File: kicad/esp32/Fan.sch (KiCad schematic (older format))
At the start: 3 parts, among them P18 Fan, Q6 IRFML8244

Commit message: 自動配線成功
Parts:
- renumbered P18 to P17
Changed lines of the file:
@@
 $Descr A4 11693 8268
 encoding utf-8
-Sheet 13 13
+Sheet 13 14
 Title ""
 Date ""
@@
 $EndComp
 $Comp
-L GND #PWR068
+L GND #PWR065
 U 1 1 58AB90DB
 P 5150 5300
-F 0 "#PWR068" H 5150 5050 50  0001 C CNN
+F 0 "#PWR065" H 5150 5050 50  0001 C CNN
 F 1 "GND" H 5150 5150 50  0000 C CNN
 F 2 "" H 5150 5300 50  0000 C CNN
@@
 Connection ~ 4750 4800
 $Comp
-L GND #PWR069
+L GND #PWR066
 U 1 1 58AB9100
 P 4750 5300
-F 0 "#PWR069" H 4750 5050 50  0001 C CNN
+F 0 "#PWR066" H 4750 5050 50  0001 C CNN
 F 1 "GND" H 4750 5150 50  0000 C CNN
 F 2 "" H 4750 5300 50  0000 C CNN
@@
 	4750 5300 4750 5200
 $Comp
-L CONN_01X02 P18
+L CONN_01X02 P17
 U 1 1 58AB920C
 P 5450 4350
-F 0 "P18" H 5450 4500 50  0000 C CNN
+F 0 "P17" H 5450 4500 50  0000 C CNN
 F 1 "Fan" V 5550 4350 50  0000 C CNN
 F 2 "mouse:SMD_conn_2" H 5450 4350 50  0001 C CNN
@@
 $EndComp
 $Comp
-L +BATT #PWR070
+L +BATT #PWR067
 U 1 1 58AB927D
 P 5150 4100
-F 0 "#PWR070" H 5150 3950 50  0001 C CNN
+F 0 "#PWR067" H 5150 3950 50  0001 C CNN
 F 1 "+BATT" H 5150 4240 50  0000 C CNN
 F 2 "" H 5150 4100 50  0000 C CNN

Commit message: 更新
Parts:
- renumbered R34 to R33
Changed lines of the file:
@@
 $EndComp
 $Comp
-L GND #PWR065
+L GND #PWR064
 U 1 1 58AB90DB
 P 5150 5300
-F 0 "#PWR065" H 5150 5050 50  0001 C CNN
+F 0 "#PWR064" H 5150 5050 50  0001 C CNN
 F 1 "GND" H 5150 5150 50  0000 C CNN
 F 2 "" H 5150 5300 50  0000 C CNN
@@
 	5150 5000 5150 5300
 $Comp
-L R R34
+L R R33
 U 1 1 58AB90F7
 P 4750 5050
-F 0 "R34" V 4830 5050 50  0000 C CNN
+F 0 "R33" V 4830 5050 50  0000 C CNN
 F 1 "10k" V 4750 5050 50  0000 C CNN
 F 2 "Resistors_SMD:R_0201" V 4680 5050 50  0001 C CNN
@@
 Connection ~ 4750 4800
 $Comp
-L GND #PWR066
+L GND #PWR065
 U 1 1 58AB9100
 P 4750 5300
-F 0 "#PWR066" H 4750 5050 50  0001 C CNN
+F 0 "#PWR065" H 4750 5050 50  0001 C CNN
 F 1 "GND" H 4750 5150 50  0000 C CNN
 F 2 "" H 4750 5300 50  0000 C CNN
@@
 $EndComp
 $Comp
-L +BATT #PWR067
+L +BATT #PWR066
 U 1 1 58AB927D
 P 5150 4100
-F 0 "#PWR067" H 5150 3950 50  0001 C CNN
+F 0 "#PWR066" H 5150 3950 50  0001 C CNN
 F 1 "+BATT" H 5150 4240 50  0000 C CNN
 F 2 "" H 5150 4100 50  0000 C CNN

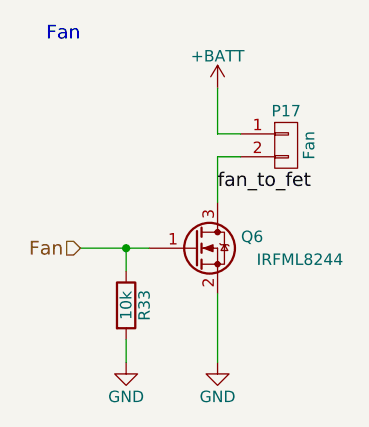
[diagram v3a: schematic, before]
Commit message: 2輪の基板を作成
部品を配置
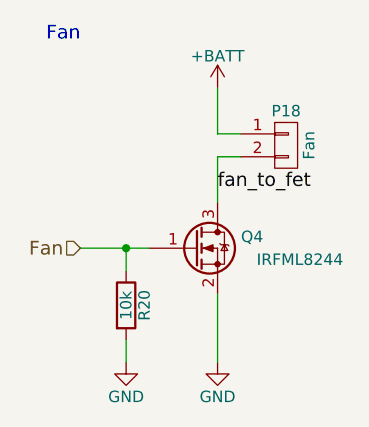
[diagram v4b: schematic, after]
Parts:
- renumbered P17 to P18, Q6 to Q4, R33 to R20
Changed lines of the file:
@@
 $Descr A4 11693 8268
 encoding utf-8
-Sheet 13 14
+Sheet 8 13
 Title ""
 Date ""
@@
 $EndDescr
 $Comp
-L Q_NMOS_GSD Q6
+L Q_NMOS_GSD Q4
 U 1 1 58AB90D4
 P 5050 4800
-F 0 "Q6" H 5350 4850 50  0000 R CNN
+F 0 "Q4" H 5350 4850 50  0000 R CNN
 F 1 "IRFML8244" H 5700 4750 50  0000 R CNN
 F 2 "TO_SOT_Packages_SMD:SOT-23" H 5250 4900 50  0001 C CNN
@@
 $EndComp
 $Comp
-L GND #PWR064
+L GND #PWR050
 U 1 1 58AB90DB
 P 5150 5300
-F 0 "#PWR064" H 5150 5050 50  0001 C CNN
+F 0 "#PWR050" H 5150 5050 50  0001 C CNN
 F 1 "GND" H 5150 5150 50  0000 C CNN
 F 2 "" H 5150 5300 50  0000 C CNN
@@
 	5150 5000 5150 5300
 $Comp
-L R R33
+L R R20
 U 1 1 58AB90F7
 P 4750 5050
-F 0 "R33" V 4830 5050 50  0000 C CNN
+F 0 "R20" V 4830 5050 50  0000 C CNN
 F 1 "10k" V 4750 5050 50  0000 C CNN
 F 2 "Resistors_SMD:R_0201" V 4680 5050 50  0001 C CNN
@@
 Connection ~ 4750 4800
 $Comp
-L GND #PWR065
+L GND #PWR051
 U 1 1 58AB9100
 P 4750 5300
-F 0 "#PWR065" H 4750 5050 50  0001 C CNN
+F 0 "#PWR051" H 4750 5050 50  0001 C CNN
 F 1 "GND" H 4750 5150 50  0000 C CNN
 F 2 "" H 4750 5300 50  0000 C CNN
@@
 	4750 5300 4750 5200
 $Comp
-L CONN_01X02 P17
+L CONN_01X02 P18
 U 1 1 58AB920C
 P 5450 4350
-F 0 "P17" H 5450 4500 50  0000 C CNN
+F 0 "P18" H 5450 4500 50  0000 C CNN
 F 1 "Fan" V 5550 4350 50  0000 C CNN
 F 2 "mouse:SMD_conn_2" H 5450 4350 50  0001 C CNN
@@
 $EndComp
 $Comp
-L +BATT #PWR066
+L +BATT #PWR052
 U 1 1 58AB927D
 P 5150 4100
-F 0 "#PWR066" H 5150 3950 50  0001 C CNN
+F 0 "#PWR052" H 5150 3950 50  0001 C CNN
 F 1 "+BATT" H 5150 4240 50  0000 C CNN
 F 2 "" H 5150 4100 50  0000 C CNN
